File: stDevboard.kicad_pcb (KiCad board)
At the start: 4 copper layers, 50 x 100 mm, 129 parts, among them IC1 MPM3610GQV-Z, IC2 IRFR9014PBF, IC3 ICM-45686, IC4 ICM-45686, IC5 MMC5983MA, J1 battery, J10 73412-0114, J11 USB_C_Receptacle_USB2.0_16P, J12 73412-0114, J13 Conn_01x04, J2 USB_C_Receptacle_USB2.0_16P, J3 Conn_02x03_Top_Bottom, Q1 IRLML6244, Q2 IRLML6244, Q3 IRLML6244, Q4 IRLML6244, Q5 IRLML6244, Q6 IRLML6244, U1 STM32U073CCUx, U2 STM32U585CIUxQ, U3 BMP581, U4 MAX-M10S, Y1 ECS-160-8-36B2-CKM-TR, Y2 CM7V-T1A-32.768KHZ, Y3 ECS-TXO-25CSMV-320-AM-TR, Y4 CM7V-T1A-32.768KHZ

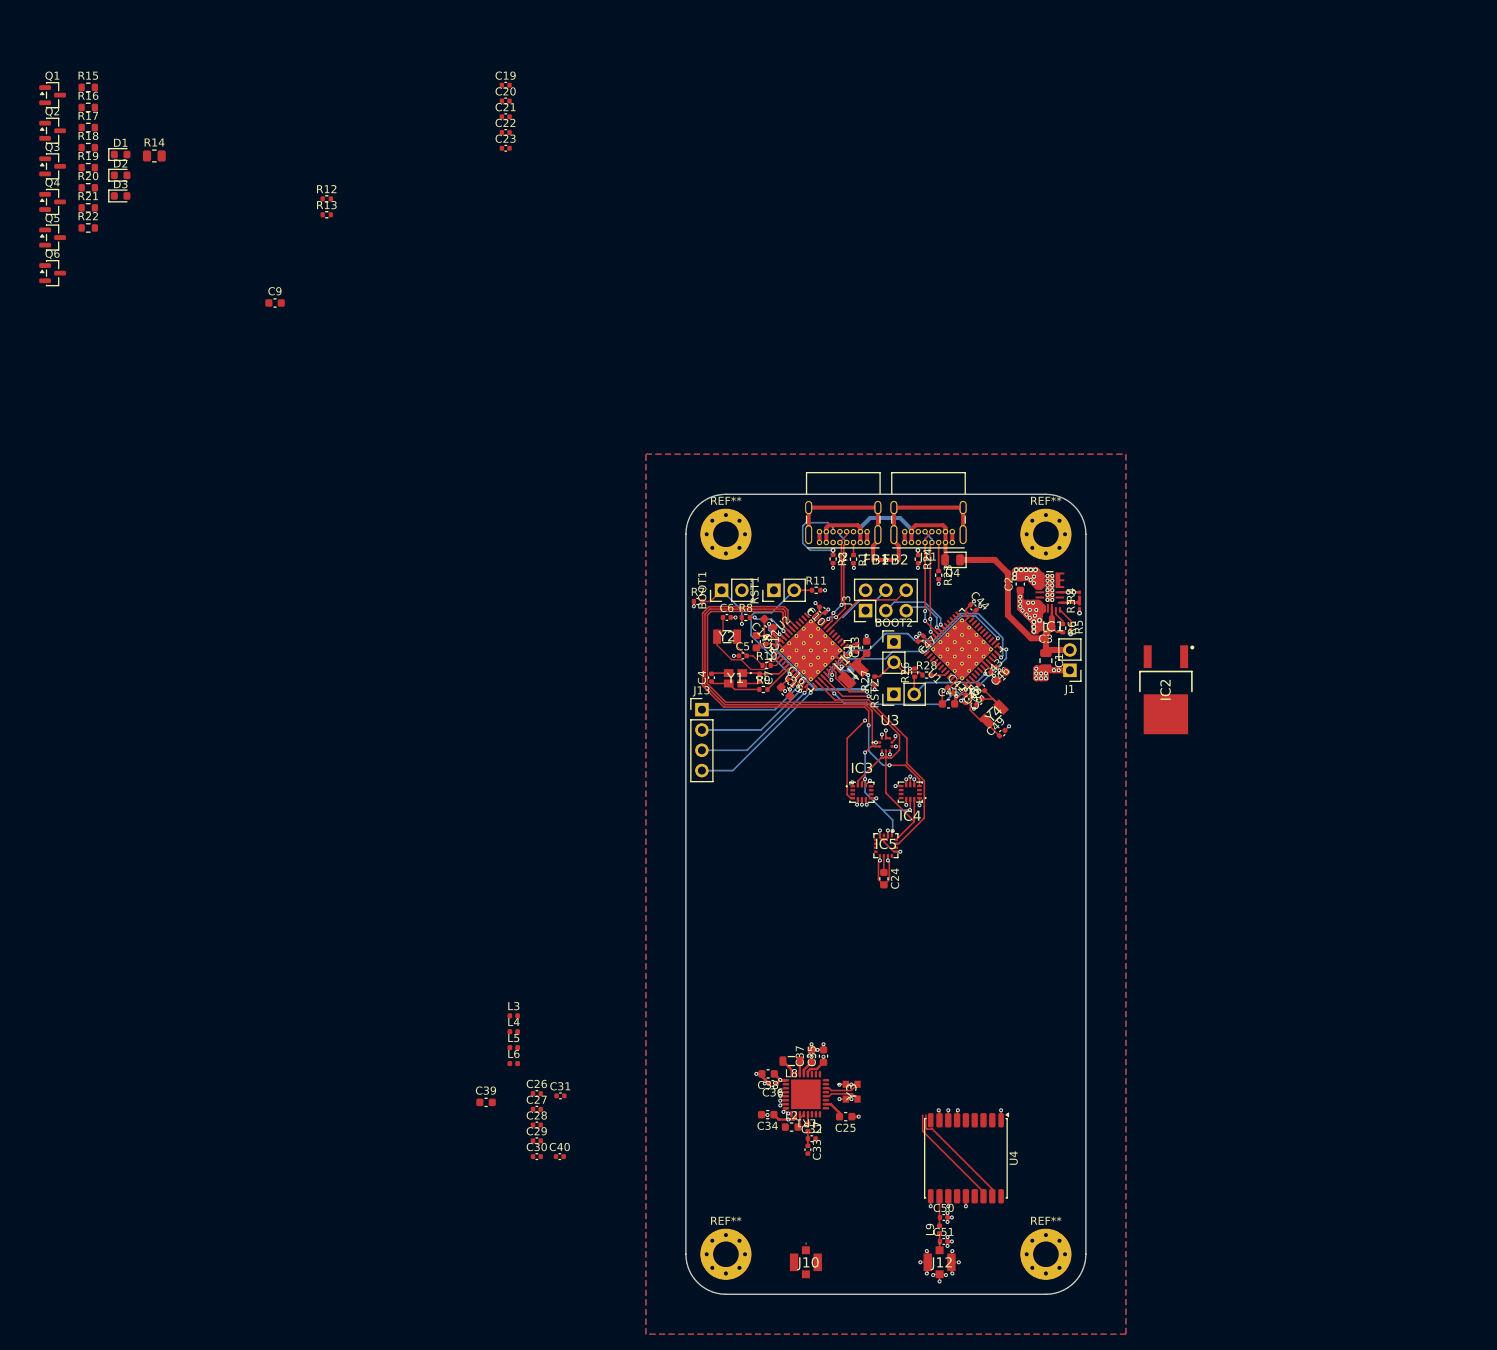
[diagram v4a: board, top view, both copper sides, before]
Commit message: basically just decoupling capacitors that I forgot
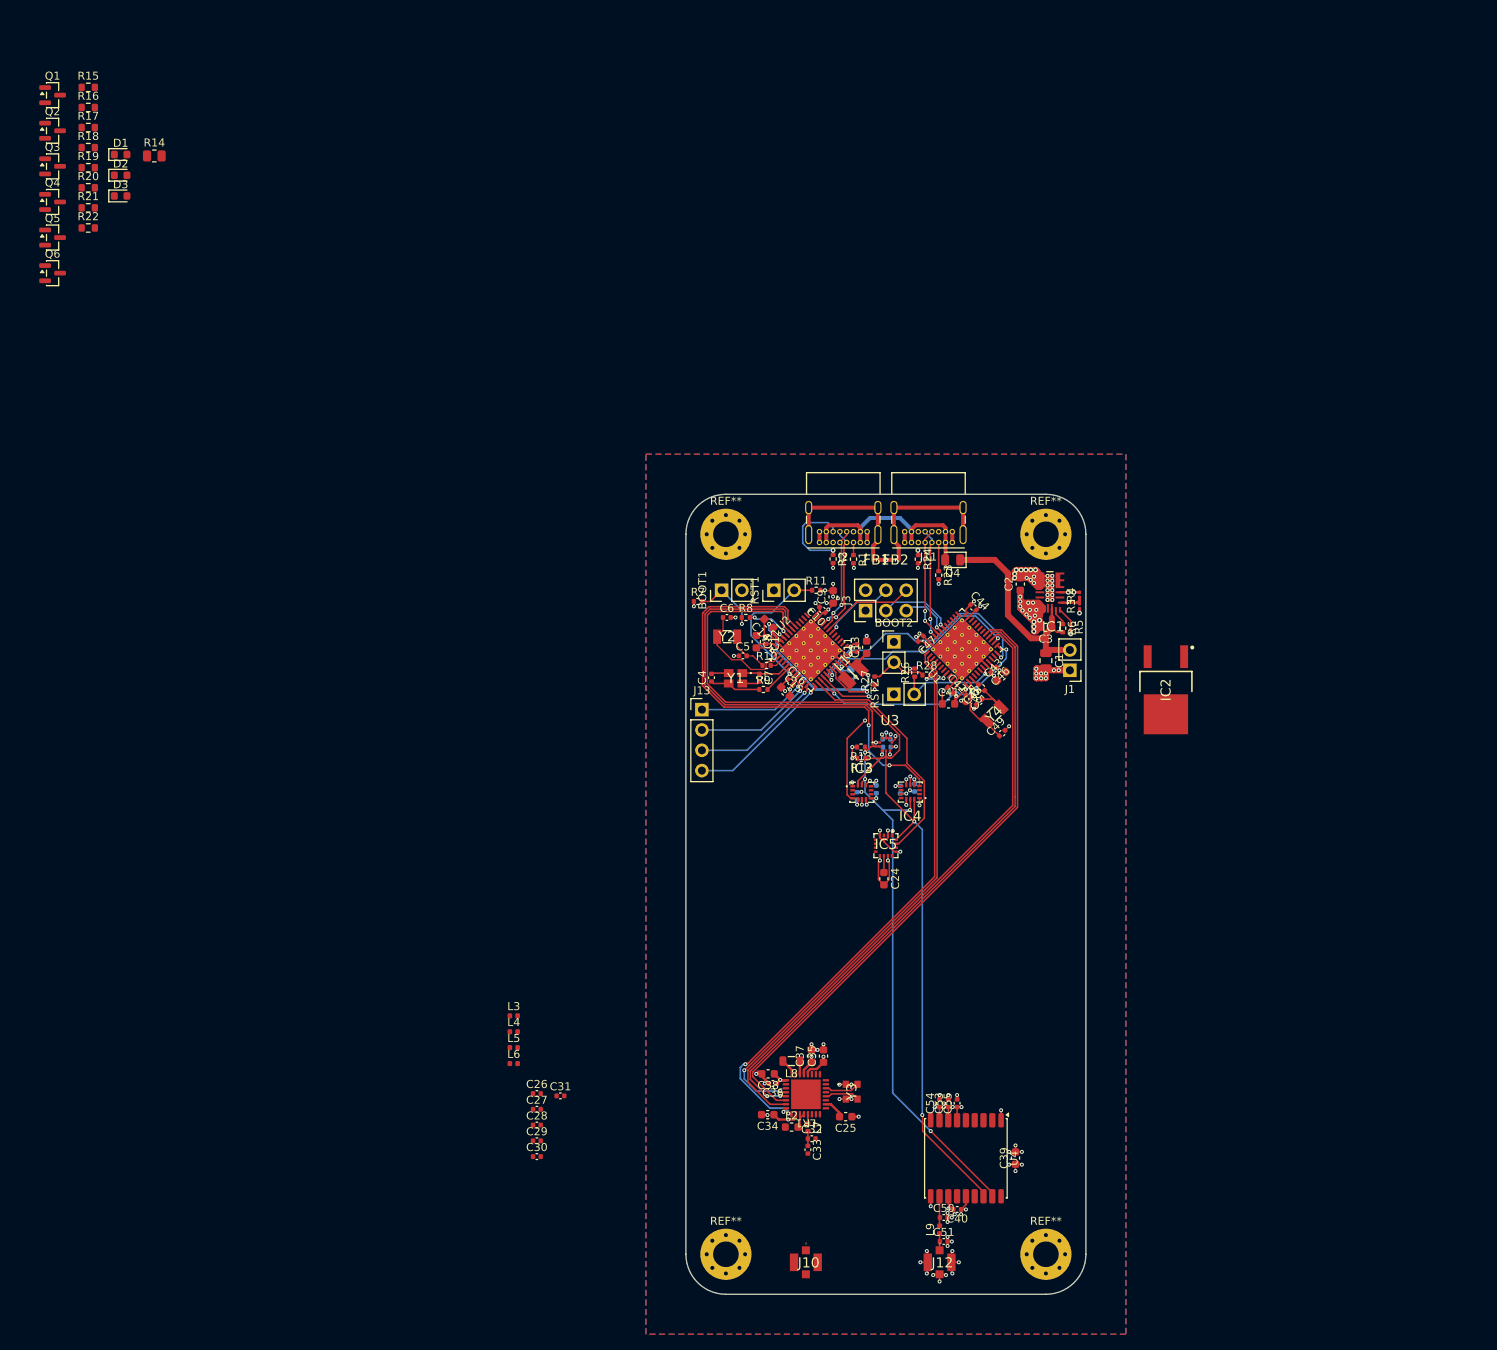
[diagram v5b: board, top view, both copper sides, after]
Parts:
- added C52: 100 nF, Capacitor_SMD:C_0402_1005Metric, B.Cu at (125.1, 106.6)
- added C53: 100nF, Capacitor_SMD:C_0402_1005Metric, F.Cu at (132.8, 151.1)
- added C54: 100nF, Capacitor_SMD:C_0402_1005Metric, F.Cu at (131.7, 151.1)
- added C55: 100nF, Capacitor_SMD:C_0402_1005Metric, F.Cu at (133.9, 151.1)
- C19, C20, C21, C22, C23: moved to B.Cu
- moved C20 97.4 mm to (121.4, 112.7), turned to 90 degrees
- moved R12 96.7 mm to (121.9, 108.0), turned to 180 degrees
- moved C22 96.5 mm to (128.6, 111.7), turned to -90 degrees
- moved C21 96.0 mm to (123.8, 111.9), turned to 90 degrees
- moved C19 94.6 mm to (125.1, 105.6), turned to 180 degrees
- moved R13 94.3 mm to (121.9, 106.6), turned to 180 degrees
- moved C23 94.1 mm to (126.8, 111.9), turned to -90 degrees
- moved C9 78.8 mm to (118.4, 87.8), turned to 90 degrees
- moved C39 66.5 mm to (141.2, 158.0), turned to 90 degrees
- moved C40 50.1 mm to (133.9, 164.4), turned to 180 degrees
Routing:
- net spi_mosi: track 0.72 -> 77.9 mm, vias 1 -> 0
- net spi_miso: track 0.72 -> 77.5 mm, vias 1 -> 2
- net spi_sclk: track 0.76 -> 77.5 mm, vias 1 -> 0
- net telem_busy: track 0.44 -> 72.5 mm, vias 1 -> 2
- net telem_rst: track 0.76 -> 69.3 mm, vias 1 -> 2
- net i2c1_sda: track 86.8 -> 125.9 mm, vias 0 -> 2
- net i2c1_sck: track 83.1 -> 120.6 mm, vias 4 -> 5
- net +3.3V: track 84.7 -> 102.5 mm, vias 45 -> 54
- net GND: track 171.3 -> 184.8 mm, vias 100 -> 114
- net mpu_tx_external: track 6.81 -> 9.29 mm, vias 0 -> 1
- net Net-(U1-PF3): track 2.12 -> 3.68 mm, vias 0 -> 2

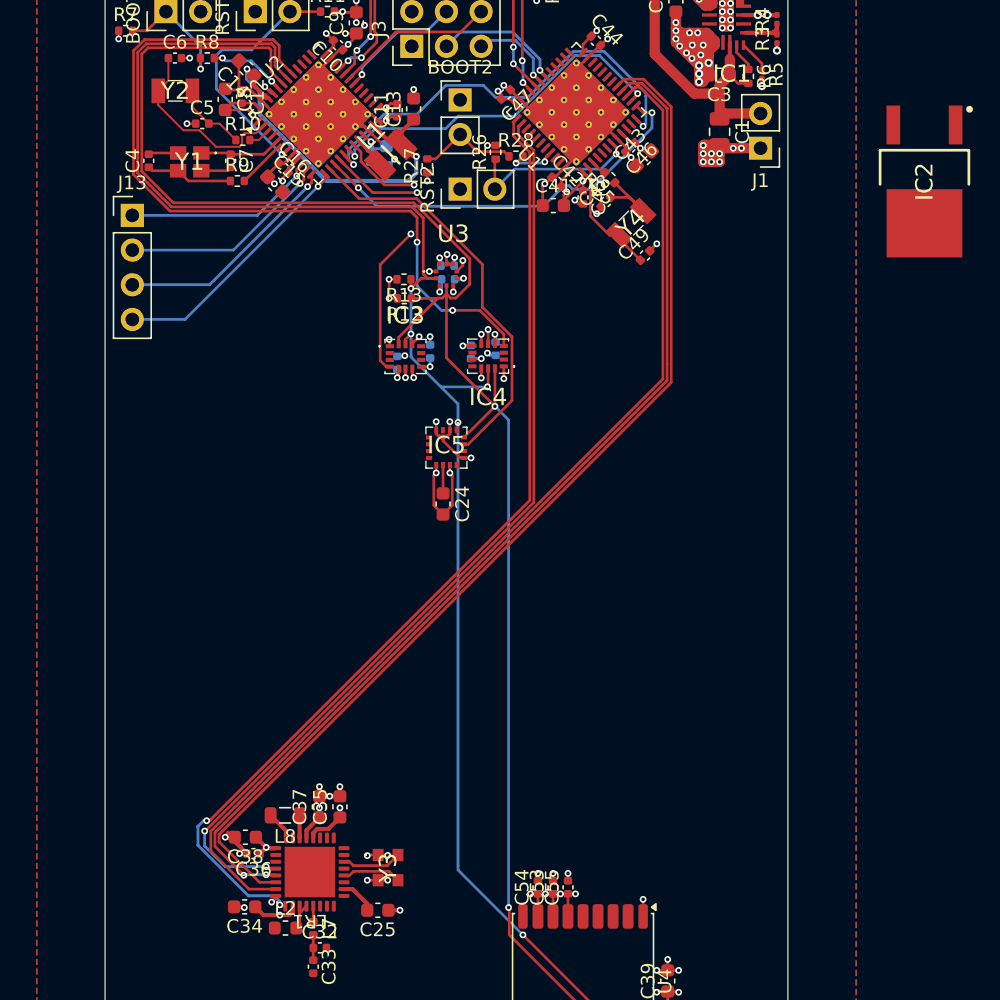
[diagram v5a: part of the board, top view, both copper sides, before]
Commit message: worked on adding mosfet stuff, last of the major signal traces routed
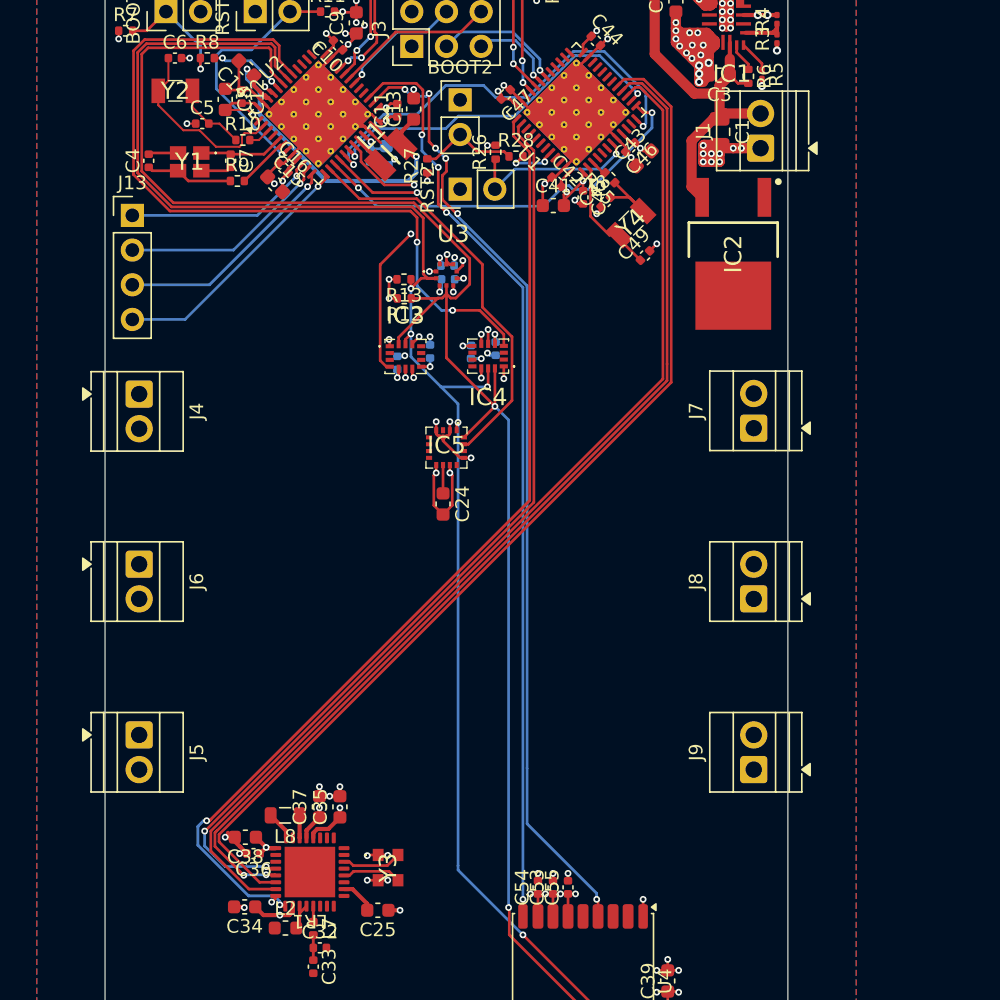
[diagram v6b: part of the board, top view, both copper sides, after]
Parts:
- added J4: Screw_Terminal_01x02, TerminalBlock:TerminalBlock_Xinya_XY308-2.54-2P_1x02_P2.54mm_Horizontal, F.Cu at (102.5, 115.0)
- added J5: Screw_Terminal_01x02, TerminalBlock:TerminalBlock_Xinya_XY308-2.54-2P_1x02_P2.54mm_Horizontal, F.Cu at (102.5, 140.0)
- added J6: Screw_Terminal_01x02, TerminalBlock:TerminalBlock_Xinya_XY308-2.54-2P_1x02_P2.54mm_Horizontal, F.Cu at (102.5, 127.5)
- added J7: Screw_Terminal_01x02, TerminalBlock:TerminalBlock_Xinya_XY308-2.54-2P_1x02_P2.54mm_Horizontal, F.Cu at (147.5, 117.5)
- added J8: Screw_Terminal_01x02, TerminalBlock:TerminalBlock_Xinya_XY308-2.54-2P_1x02_P2.54mm_Horizontal, F.Cu at (147.5, 130.0)
- added J9: Screw_Terminal_01x02, TerminalBlock:TerminalBlock_Xinya_XY308-2.54-2P_1x02_P2.54mm_Horizontal, F.Cu at (147.5, 142.5)
- J1: footprint Connector_PinHeader_2.54mm:PinHeader_1x02_P2.54mm_Vertical -> TerminalBlock:TerminalBlock_Xinya_XY308-2.54-2P_1x02_P2.54mm_Horizontal
- moved IC2 15.0 mm to (146.0, 104.8)
- turned J1 to 90 degrees
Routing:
- net gps_pulse: track 0.00 -> 70.6 mm, vias 0 -> 6
- net gps_rst: track 0.00 -> 68.3 mm, vias 0 -> 4
- net +BATT: track 28.5 -> 35.7 mm

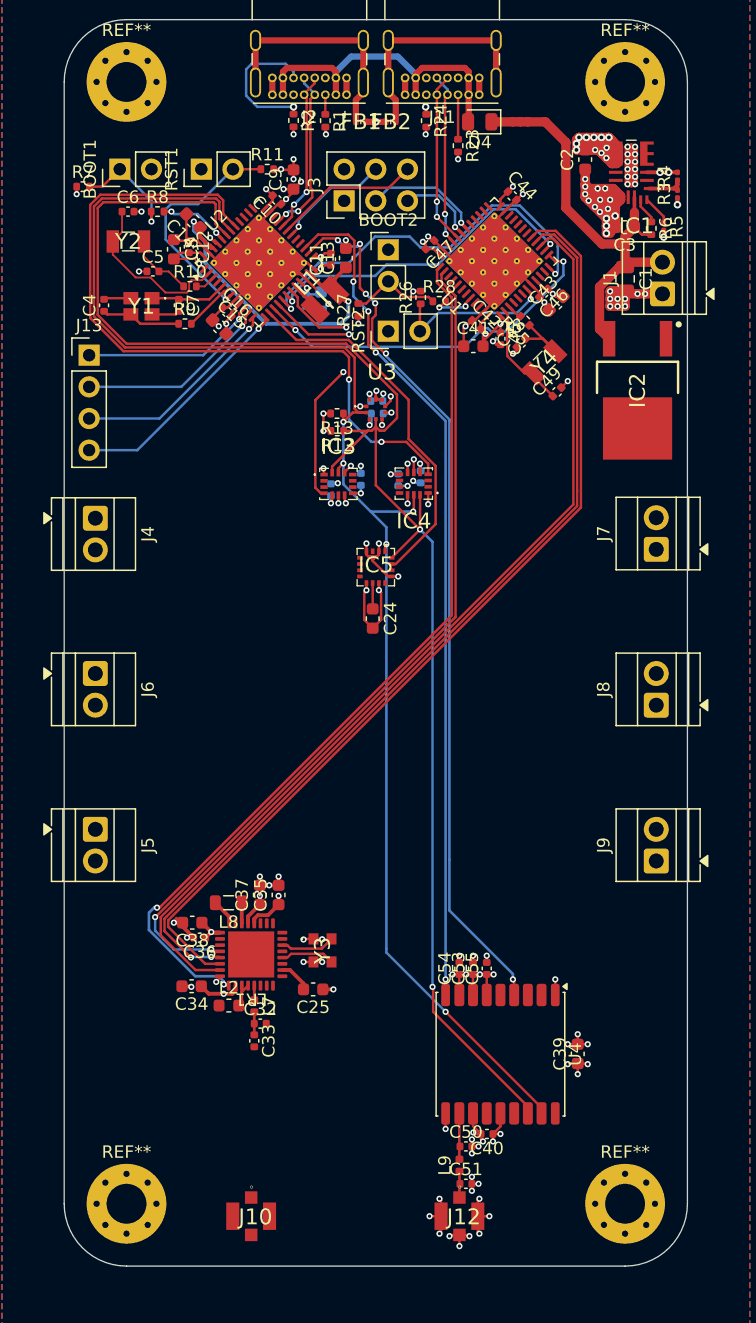
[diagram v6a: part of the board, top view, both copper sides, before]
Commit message: added in the flash chip and micro sd card, rerouted some stuff, looking real nice rn - still need to finish rf, pyros, and add in the piezo
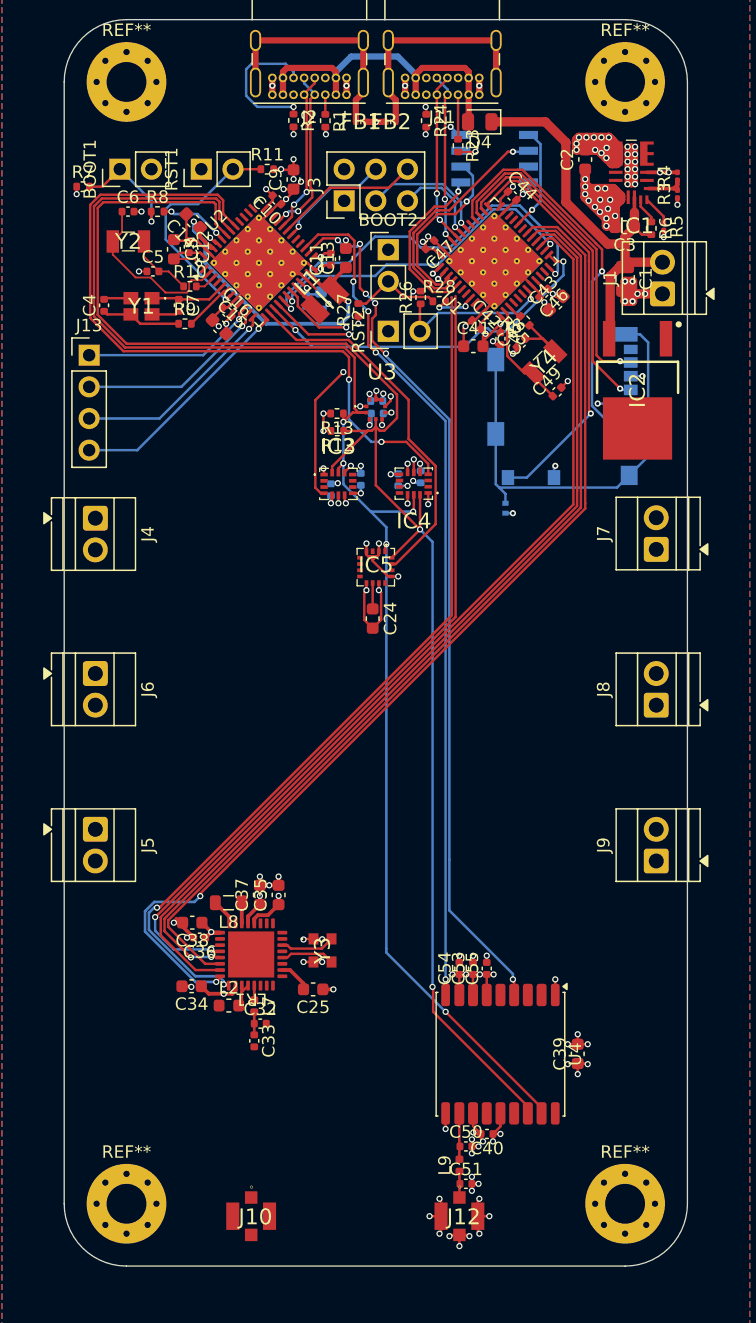
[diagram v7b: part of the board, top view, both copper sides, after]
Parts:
- added FB3: BLM15AX102SN1D, footprints:NFZ15SG152SN10B, B.Cu at (135.4, 114.2)
- added IC6: AT25SF041B-SSHB-B, footprints:SOIC127P600X175-8N, B.Cu at (134.5, 86.2)
- added J14: Micro_SD_Card_Det2, Connector_Card:microSD_HC_Molex_104031-0811, B.Cu at (140.0, 106.0)
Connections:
- IC1 pad 19: unconnected-(IC1-SW_4-Pad19) -> /shutupdrc
- IC1 pad 4: unconnected-(IC1-SW_1-Pad4) -> /shutupdrc
- IC1 pad 5: unconnected-(IC1-SW_2-Pad5) -> /shutupdrc
- IC1 pad 6: unconnected-(IC1-SW_3-Pad6) -> /shutupdrc
- LR1 pad 24: GND -> spi_nss
- U1 pad 18: unconnected-(U1-PB0-Pad18) -> spi_nss
- U1 pad 20: unconnected-(U1-PB2-Pad20) -> /peripheral micro/flash_cs
- U1 pad 25: unconnected-(U1-PB12-Pad25) -> /peripheral micro/sd_det
- U1 pad 26: unconnected-(U1-PB13-Pad26) -> /peripheral micro/sd_clk
- U1 pad 27: unconnected-(U1-PB14-Pad27) -> /peripheral micro/sd_miso
- U1 pad 28: unconnected-(U1-PB15-Pad28) -> /peripheral micro/sd_mosi
- U1 pad 39: unconnected-(U1-PB3-Pad39) -> /peripheral micro/flash_clk
- U1 pad 40: unconnected-(U1-PB4-Pad40) -> /peripheral micro/flash_miso
- U1 pad 41: unconnected-(U1-PB5-Pad41) -> /peripheral micro/flash_mosi
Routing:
- net spi_nss: track 0.00 -> 84.6 mm, vias 0 -> 2
- net Net-(J14-SHIELD): track 0.00 -> 36.0 mm
- net /peripheral micro/sd_det: track 0.00 -> 33.2 mm, vias 0 -> 1
- net /peripheral micro/sd_mosi: track 0.00 -> 32.1 mm, vias 0 -> 1
- net /peripheral micro/sd_clk: track 0.00 -> 25.9 mm, vias 0 -> 1
- net /peripheral micro/sd_miso: track 0.00 -> 25.7 mm, vias 0 -> 1
- net /peripheral micro/flash_miso: track 0.00 -> 18.9 mm, vias 0 -> 1
- net /peripheral micro/flash_clk: track 0.00 -> 14.7 mm, vias 0 -> 1
- net /peripheral micro/flash_mosi: track 0.00 -> 14.0 mm, vias 0 -> 1
- net /peripheral micro/flash_cs: track 0.00 -> 8.65 mm, vias 0 -> 1
- net +3.3V: track 102.5 -> 107.2 mm, vias 54 -> 57
- net telem_busy: track 72.5 -> 70.3 mm, vias 2 -> 3
- net telem_rst: track 69.3 -> 67.6 mm, vias 2 -> 3
- net GND: track 184.8 -> 183.5 mm, vias 114 -> 115
- net ppu_rx_external: track 6.52 -> 7.50 mm
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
